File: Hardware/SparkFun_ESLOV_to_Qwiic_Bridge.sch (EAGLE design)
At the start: 12 parts, among them J2 QWIIC_RA, U1 3.3V

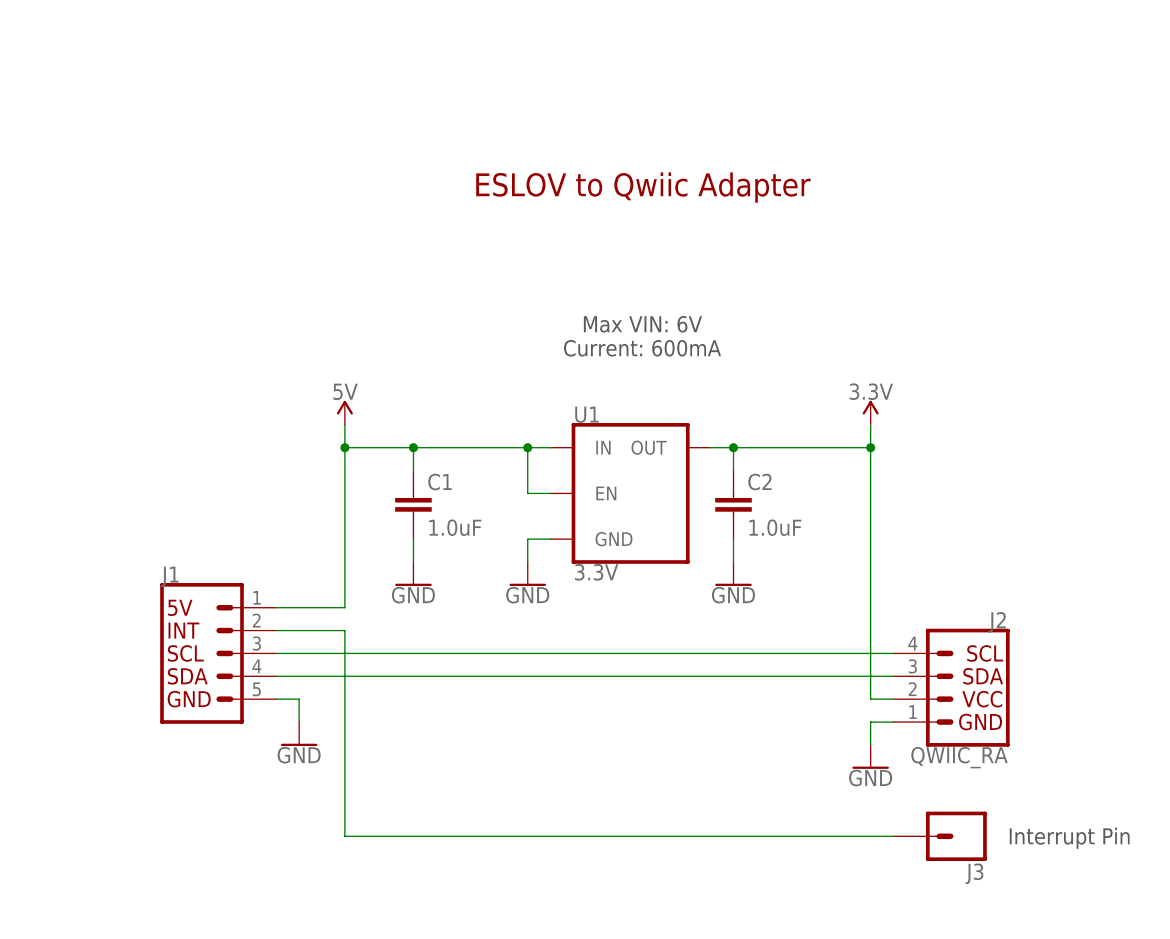
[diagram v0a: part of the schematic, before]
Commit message: Rename Board File
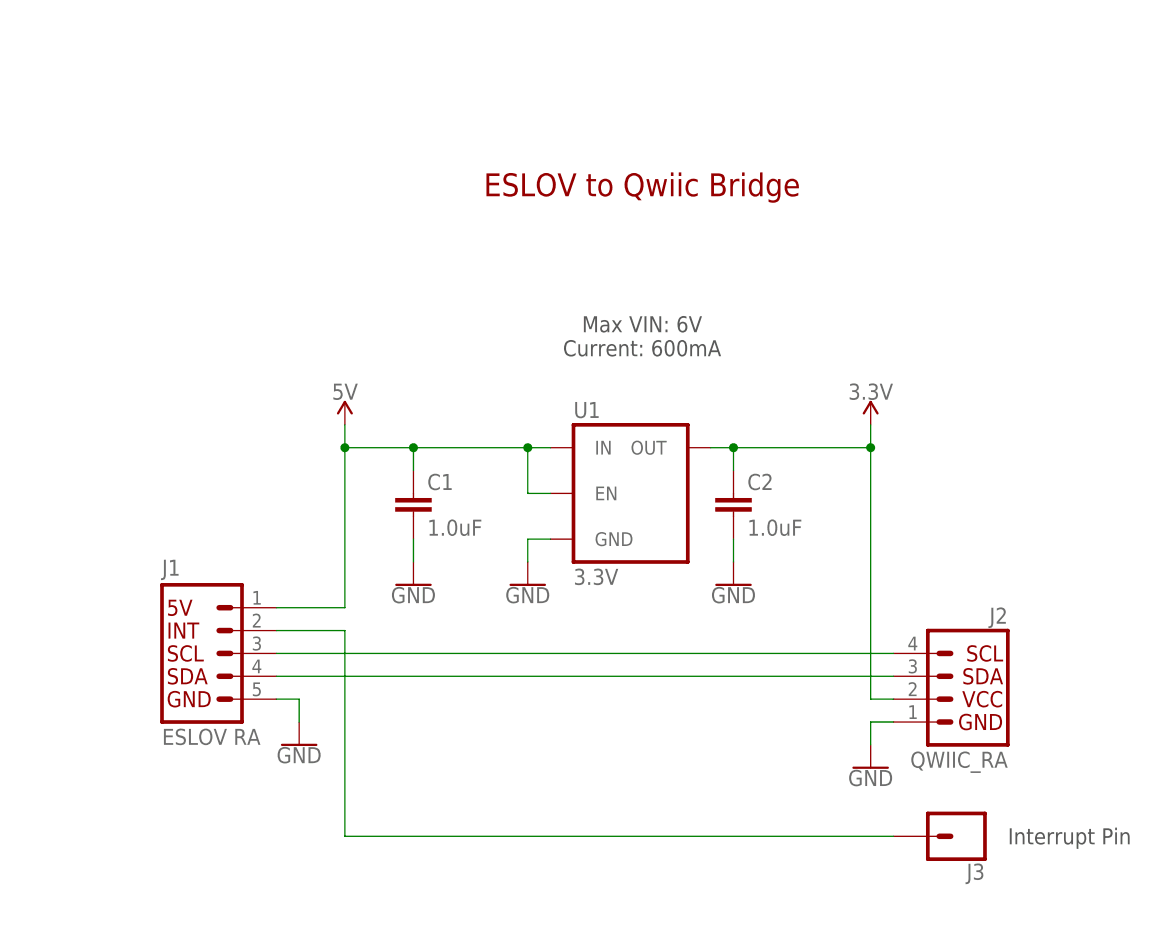
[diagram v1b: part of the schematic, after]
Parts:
- J1: value (none) -> ESLOV RA
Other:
- note added: "ESLOV to Qwiic Bridge"
- note removed: "ESLOV to Qwiic Adapter"
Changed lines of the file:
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@@
 <attribute name="REV" value="v10"/>
 </part>
-<part name="J1" library="ESLOV" deviceset="ESLOV" device=""/>
+<part name="J1" library="ESLOV" deviceset="ESLOV" device="" value="ESLOV RA"/>
 <part name="U1" library="SparkFun-IC-Power" deviceset="V_REG_AP2112" device="K-3.3V" value="3.3V"/>
 <part name="J2" library="SparkFun-Connectors" deviceset="QWIIC_CONNECTOR" device="JS-1MM" value="QWIIC_RA"/>
@@
 <sheet>
 <plain>
-<text x="124.46" y="149.86" size="2.54" layer="94" font="vector" align="bottom-center">ESLOV to Qwiic Adapter</text>
+<text x="124.46" y="149.86" size="2.54" layer="94" font="vector" align="bottom-center">ESLOV to Qwiic Bridge</text>
 <text x="165.1" y="78.74" size="1.778" layer="97" font="vector" align="center-left">Interrupt Pin</text>
 <text x="124.46" y="132.08" size="1.778" layer="97" font="vector" align="bottom-center">Max VIN: 6V
@@
 </instance>
 <instance part="J1" gate="G$1" x="76.2" y="99.06" smashed="yes">
-<attribute name="VALUE" x="71.12" y="91.186" size="1.778" layer="96" font="vector" align="top-left"/>
-<attribute name="NAME" x="71.12" y="106.934" size="1.778" layer="95" font="vector"/>
+<attribute name="VALUE" x="71.12" y="90.678" size="1.778" layer="96" font="vector" align="top-left"/>
+<attribute name="NAME" x="71.12" y="107.696" size="1.778" layer="95" font="vector"/>
 </instance>
 <instance part="U1" gate="G$1" x="124.46" y="116.84" smashed="yes">
-<attribute name="NAME" x="116.84" y="124.714" size="1.778" layer="95" font="vector"/>
-<attribute name="VALUE" x="116.84" y="108.966" size="1.778" layer="96" font="vector" align="top-left"/>
+<attribute name="NAME" x="116.84" y="125.222" size="1.778" layer="95" font="vector"/>
+<attribute name="VALUE" x="116.84" y="108.458" size="1.778" layer="96" font="vector" align="top-left"/>
 </instance>
 <instance part="J2" gate="J1" x="160.02" y="93.98" smashed="yes" rot="MR0">
-<attribute name="VALUE" x="165.1" y="88.646" size="1.778" layer="96" font="vector" rot="MR0" align="top-left"/>
-<attribute name="NAME" x="165.1" y="101.854" size="1.778" layer="95" font="vector" rot="MR0"/>
+<attribute name="VALUE" x="165.1" y="88.138" size="1.778" layer="96" font="vector" rot="MR0" align="top-left"/>
+<attribute name="NAME" x="165.1" y="102.362" size="1.778" layer="95" font="vector" rot="MR0"/>
 </instance>
 <instance part="J3" gate="J1" x="160.02" y="78.74" smashed="yes" rot="R180">
